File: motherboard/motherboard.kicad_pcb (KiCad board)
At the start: 4 copper layers, 158.5 x 92 mm, 270 parts, among them CN1 PJ-332A-6A (3.5mm Jack), IC1 PI6C557-05BLE, J1 USB_C_Receptacle, J10 DEBUG UART, J11 SYSTEM, J12 5V FAN, J13 Bus_M.2_Socket_E, J14 Micro_SD_Card_Det1, J15 Bus_M.2_Socket_M, J16 USB, J17 USB, J18 USB, J19 USB, J2 20455-040E-76 OLED IPEX, J20 CM3588 Hirose Connector, J21 5V IN, J22 BATTERY IN, J3 RIGHT SPEAKERS, J4 LEFT SPEAKERS, J5 Outer USB-C, J6 OLED EL POWER, J7 HALL SWITCH, J8 HDMI_A, J9 Inner USB-C, Q1 2SK3018W, Q10 2SK3018W, Q11 AO3415A, Q12 2SK3018W, Q2 2SK3018W, Q3 L2N7002WT1G, Q4 2SK3018W, Q5 2SK3018W, Q6 WNM6002-3/TR, Q7 WNM6002-3/TR, Q8 WNM6002-3/TR, Q9 WNM6002-3/TR, SW1 PWR, SW2 RESET, SW3 MASK, SW4 RECOVERY, U1 TPD4E02B04, U10 TPD4E02B04, U11 TPD4E02B04, U12 TPD4E02B04, U13 TPD4E02B04, U14 AP2331, U15 TVS2200DRV, U18 TPD4E02B04, U19 TPD4E02B04, U2 TPD4E02B04, U20 TPS54331DR, U21 AP2127K-3.3, U22 CH334F, U23 TPA2028D1YZFT, U25 TPA2028D1YZFT, U26 AMS1117-1.8, U27 TPS54331DR, U28 SPI Flash, U29 TVS2200DRV, U3 TPD4E02B04, U4 FUSB302BMPX, U5 SY6280AAC, U6 SY6280AAC, U7 FUSB302BMPX, U8 TPD4E02B04, U9 TPD4E02B04, Y1 25MHz, Y2 12MHz

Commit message: routing work
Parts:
- moved R4 11.8 mm to (100.4, 123.7), turned to 90 degrees
- moved C23 1.33 mm to (67.7, 88.2), turned to 0 degrees
- moved R5 0.79 mm to (100.6, 136.7), turned to 180 degrees
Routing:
- net +1V8: track 0.00 -> 37.3 mm, vias 0 -> 2
- net /HDMI_TX/HDMI0_5V: track 0.00 -> 30.3 mm
- net /USBC0/CC1: track 0.00 -> 23.7 mm, vias 0 -> 2
- net /Audio/L_DET: track 0.00 -> 23.0 mm, vias 0 -> 2
- net /USBC0/CC2: track 0.00 -> 22.1 mm, vias 0 -> 2
- net /HDMI_TX/CEC: track 0.00 -> 20.9 mm, vias 0 -> 2
- net Net-(J1-SHIELD): track 0.00 -> 20.7 mm
- net unconnected-(R1-Pad1): track 0.00 -> 19.2 mm
- net /HDMI_TX/SCL: track 0.00 -> 19.2 mm, vias 0 -> 2
- net /USBC1/VBUS: track 7.74 -> 26.9 mm, vias 0 -> 2
- net /USBC1/CC1: track 0.00 -> 18.2 mm, vias 0 -> 2
- net /USBC1/CC2: track 0.00 -> 17.7 mm, vias 0 -> 2
- net /HDMI_TX/SDA: track 0.00 -> 16.2 mm, vias 0 -> 2
- net /USBC0/SBUS2: track 0.00 -> 12.8 mm, vias 0 -> 2
- net /Audio/L_AUDIO: track 0.00 -> 12.8 mm, vias 0 -> 3
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- removed copper zone on F.Cu, net /USBC1/VBUS

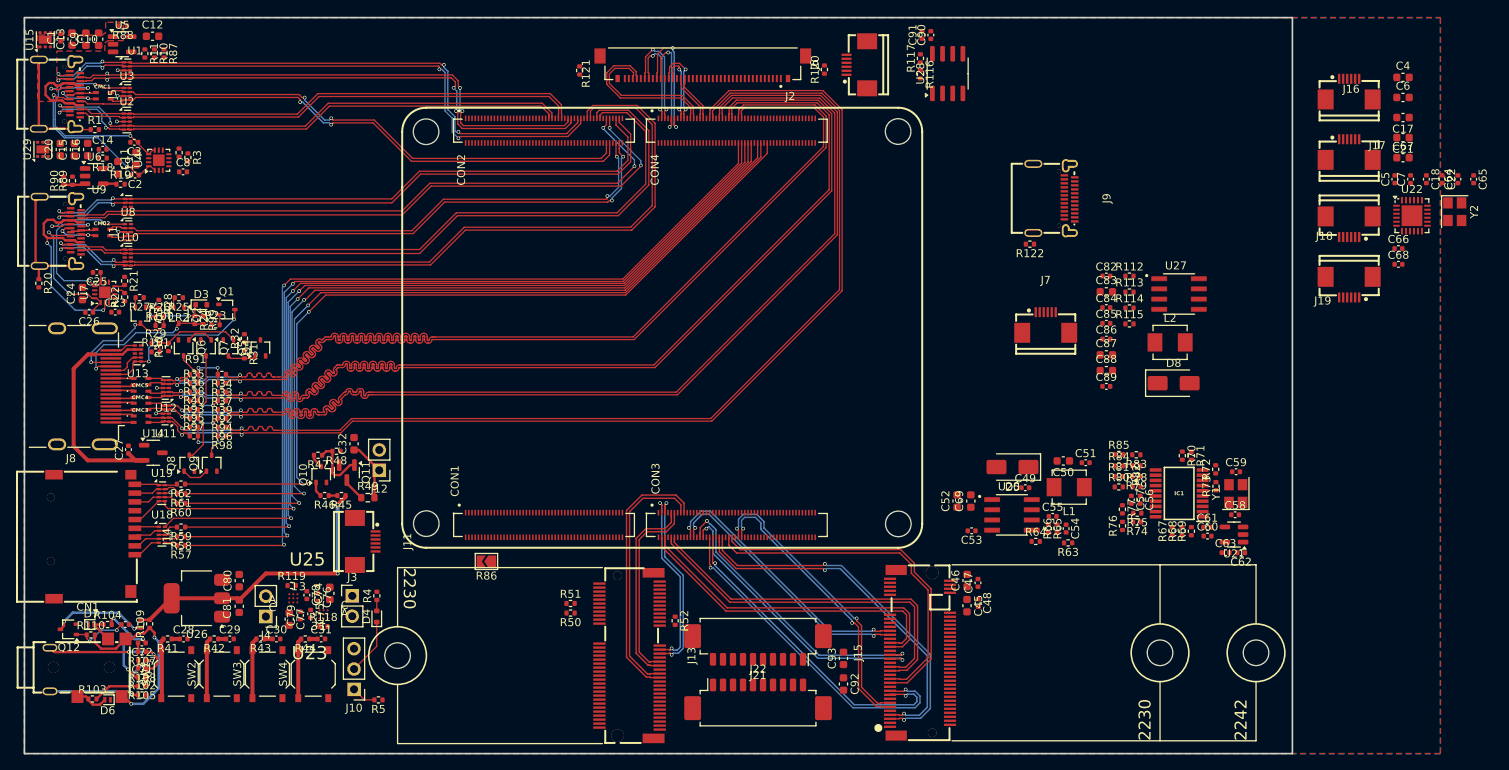
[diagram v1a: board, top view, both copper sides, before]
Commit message: added two more display eval test boards
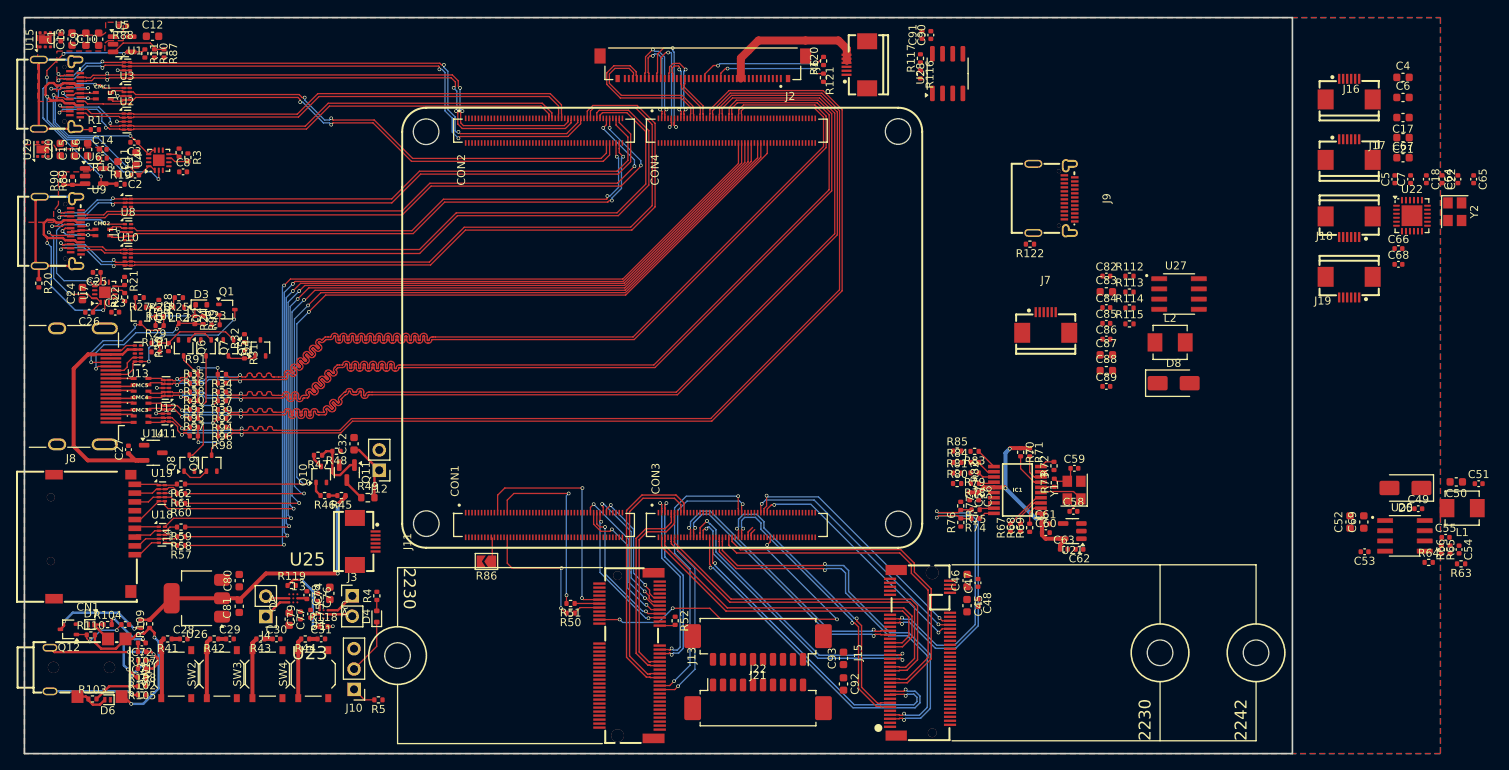
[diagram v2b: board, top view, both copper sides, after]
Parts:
- moved C49 49.2 mm to (230.6, 112.8)
- moved C50 49.2 mm to (235.3, 109.5)
- moved C51 49.2 mm to (238.1, 109.7)
- moved C52 49.2 mm to (222.1, 114.5)
- moved C53 49.2 mm to (223.9, 118.2)
- moved C54 49.2 mm to (235.7, 117.9)
- moved C55 49.2 mm to (234.0, 116.4)
- moved C69 49.2 mm to (223.8, 114.5)
- moved D5 49.2 mm to (229.0, 110.2)
- moved L1 49.2 mm to (236.1, 112.7)
- moved R63 49.2 mm to (235.9, 119.7)
- moved R64 49.2 mm to (231.9, 119.5)
- moved R65 49.2 mm to (233.5, 117.9)
- moved R66 49.2 mm to (234.6, 117.9)
- moved U20 49.2 mm to (228.9, 116.2)
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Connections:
- C45 pad 1: /PCIE3.0-MKEY/+3.3V_PCIE -> +3.3V_PCIE
- C46 pad 1: /PCIE3.0-MKEY/+3.3V_PCIE -> +3.3V_PCIE
- C47 pad 1: /PCIE3.0-MKEY/+3.3V_PCIE -> +3.3V_PCIE
- C48 pad 1: /PCIE3.0-MKEY/+3.3V_PCIE -> +3.3V_PCIE
- C50 pad 1: /PCIE3.0-MKEY/+3.3V_PCIE -> +3.3V_PCIE
- C51 pad 1: /PCIE3.0-MKEY/+3.3V_PCIE -> +3.3V_PCIE
- J13 pad 2: /PCIE2.0-EKEY/EKEY_3.3V -> +3.3V_PCIE
- J13 pad 4: /PCIE2.0-EKEY/EKEY_3.3V -> +3.3V_PCIE
- J13 pad 72: /PCIE2.0-EKEY/EKEY_3.3V -> +3.3V_PCIE
- J13 pad 74: /PCIE2.0-EKEY/EKEY_3.3V -> +3.3V_PCIE
- J15 pad 12: /PCIE3.0-MKEY/+3.3V_PCIE -> +3.3V_PCIE
- J15 pad 14: /PCIE3.0-MKEY/+3.3V_PCIE -> +3.3V_PCIE
- J15 pad 16: /PCIE3.0-MKEY/+3.3V_PCIE -> +3.3V_PCIE
- J15 pad 18: /PCIE3.0-MKEY/+3.3V_PCIE -> +3.3V_PCIE
- J15 pad 2: /PCIE3.0-MKEY/+3.3V_PCIE -> +3.3V_PCIE
- J15 pad 4: /PCIE3.0-MKEY/+3.3V_PCIE -> +3.3V_PCIE
- J15 pad 70: /PCIE3.0-MKEY/+3.3V_PCIE -> +3.3V_PCIE
- J15 pad 72: /PCIE3.0-MKEY/+3.3V_PCIE -> +3.3V_PCIE
- J15 pad 74: /PCIE3.0-MKEY/+3.3V_PCIE -> +3.3V_PCIE
- L1 pad 1: /PCIE3.0-MKEY/+3.3V_PCIE -> +3.3V_PCIE
- R63 pad 1: /PCIE3.0-MKEY/+3.3V_PCIE -> +3.3V_PCIE
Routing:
- net /GPIO0_C5/UART0_TX_M0/PWM4_M0: track 0.00 -> 45.2 mm, vias 0 -> 4
- net /PCIE3.0-MKEY/PCIE30_REFCLK_A_N: track 0.00 -> 37.1 mm, vias 0 -> 2
- net /GPIO4_A1/TP_2_RST_L: track 0.00 -> 36.1 mm, vias 0 -> 2
- net /GPIO4_A0/TP_2_INT_L: track 0.00 -> 35.9 mm, vias 0 -> 2
- net /PCIE3.0-MKEY/PCIE30_REFCLK_A_P: track 0.00 -> 35.8 mm, vias 0 -> 2
- net /GPIO4_B5/PCIE30X4_WAKEn_M1_L: track 0.00 -> 31.7 mm, vias 0 -> 2
- net /GPIO4_B4/PCIE30X4_CLKREQn_M1_L: track 0.00 -> 31.3 mm, vias 0 -> 2
- net /GPIO1_D2/TYPEC5V_PWREN_H: track 1.67 -> 32.7 mm, vias 0 -> 4
- net /GPIO4_B6/PCIE30X4_PERSTn_M1_L: track 0.00 -> 30.4 mm, vias 0 -> 2
- net /GPIO2_C0: track 0.00 -> 29.0 mm, vias 0 -> 2
- net /PCIE3.0-MKEY/+3.3V_PI6C: track 0.00 -> 25.7 mm, vias 0 -> 3
- net /GPIO2_C3: track 0.00 -> 23.5 mm, vias 0 -> 2
- net /USBC0/VBUS: track 12.2 -> 33.2 mm, vias 0 -> 2
- net Net-(J6-Pin_4): track 0.00 -> 18.6 mm
- net /GPIO2_A6: track 0.00 -> 17.9 mm, vias 0 -> 2
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- added copper zone on F.Cu, net /USBC1/VBUS

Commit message: starting motherboard v0.2
lessons from display eval v1
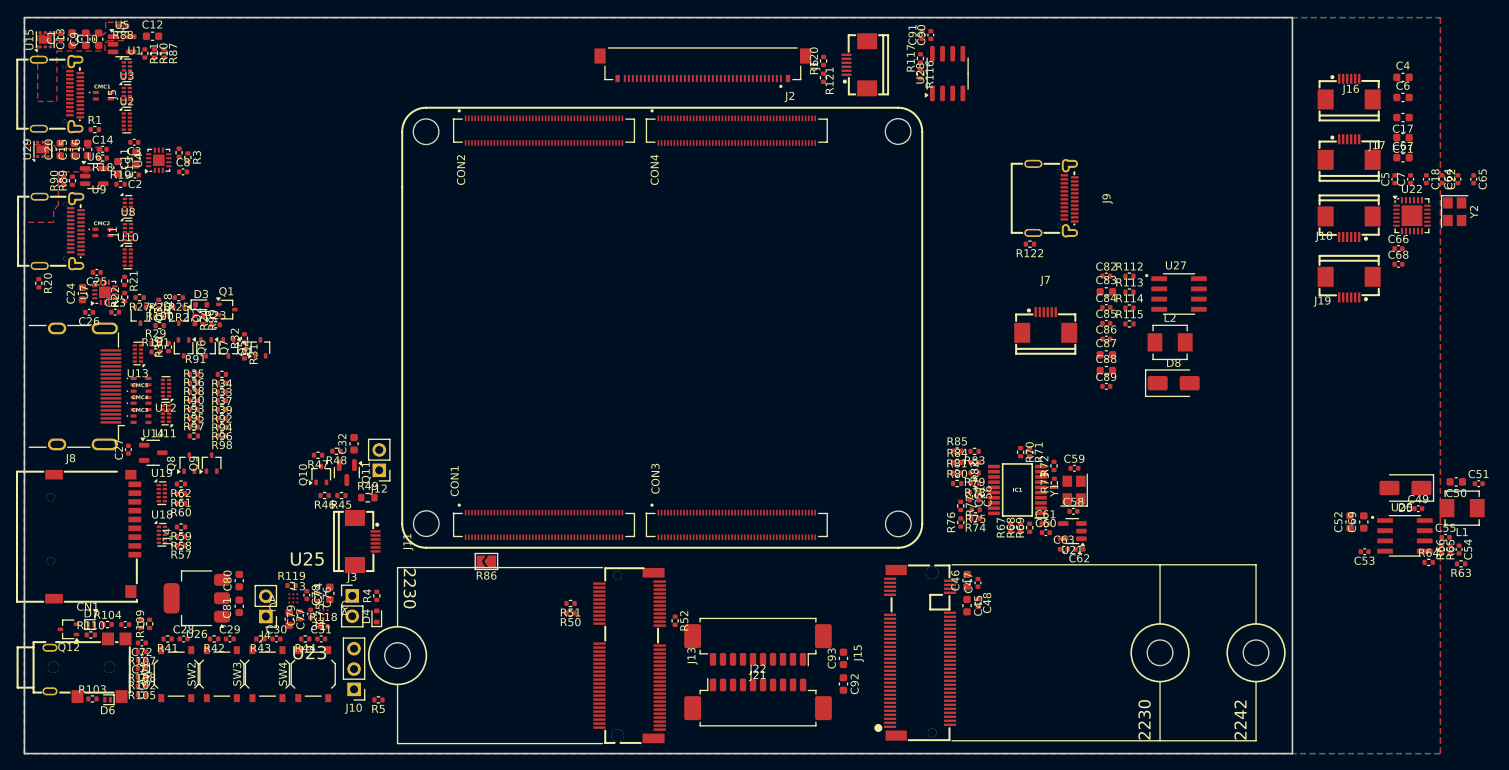
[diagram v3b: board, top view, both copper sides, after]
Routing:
- net /HDMI_TX/HDMI0_TX1P: track 141.2 -> 0.00 mm, vias 2 -> 0
- net /HDMI_TX/HDMI0_TX2P: track 141.1 -> 0.00 mm, vias 2 -> 0
- net /HDMI_TX/HDMI0_TX0P: track 141.0 -> 0.00 mm, vias 2 -> 0
- net /HDMI_TX/HDMI0_TX1N: track 140.9 -> 0.00 mm, vias 2 -> 0
- net /HDMI_TX/HDMI0_TX0N: track 140.8 -> 0.00 mm, vias 2 -> 0
- net /HDMI_TX/HDMI0_TX2N: track 140.7 -> 0.00 mm, vias 2 -> 0
- net /HDMI_TX/HDMI0_TX3P: track 140.5 -> 0.00 mm, vias 2 -> 0
- net /HDMI_TX/HDMI0_TX3N: track 140.2 -> 0.00 mm, vias 2 -> 0
- net /SD Card/CLK: track 114.4 -> 0.00 mm, vias 2 -> 0
- net /SD Card/VDD: track 113.6 -> 0.00 mm, vias 2 -> 0
- net /SDMMC0_D2: track 110.6 -> 0.00 mm, vias 2 -> 0
- net /SDMMC0_D3: track 109.7 -> 0.00 mm, vias 2 -> 0
- net /SDMMC0_CMD: track 108.5 -> 0.00 mm, vias 2 -> 0
- net /SDMMC0_D0: track 106.6 -> 0.00 mm, vias 2 -> 0
- net /SDMMC0_D1: track 105.8 -> 0.00 mm, vias 2 -> 0
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
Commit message: v0.2 layout
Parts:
- removed C54, C85: 1nF, Capacitor_SMD:C_0402_1005Metric
- removed C55, C86: 10pF, Capacitor_SMD:C_0402_1005Metric
- removed C69, C77, C83, C87, C88, C92, C93: 10uF, Capacitor_SMD:C_0603_1608Metric
- removed C78, C79, C84: 1uF, Capacitor_SMD:C_0402_1005Metric
- removed C82: 100nF, Capacitor_SMD:C_0402_1005Metric
- removed C89: 8.2nF, Capacitor_SMD:C_0402_1005Metric
- removed D5, D8: SS54, Diode_SMD:D_SMA
- removed J21: 5V IN, Connector_Molex:Molex_PicoBlade_53261-1071_1x10-1MP_P1.25mm_Horizontal
- removed J9: Inner USB-C, USB-C:USB-C-SMD_TYPE-C-24P-QT
- removed R112, R65: 24k, Resistor_SMD:R_0402_1005Metric
- removed R113, R66: 2k, Resistor_SMD:R_0402_1005Metric
- removed R114, R63: 10k, Resistor_SMD:R_0402_1005Metric
- removed R115, R64: 3.3k, Resistor_SMD:R_0402_1005Metric
- removed R118, R119, R120, R121: 0R, Resistor_SMD:R_0402_1005Metric
- removed R122: 1M, Resistor_SMD:R_0402_1005Metric
- removed U25: TPA2028D1YZFT, Audio_Amp:BGA9C50P3X3_162X162X63
- removed U27: TPS54331DR, TPS54331DR:SOIC127P599X175-8N
- added 10k: Resistor_SMD:R_0402_1005Metric, Resistor_SMD:R_0402_1005Metric, F.Cu at (171.8, 118.4)
- added C33: 1uF, Capacitor_SMD:C_0402_1005Metric, F.Cu at (170.9, 54.3)
- added C34: 1uF, Capacitor_SMD:C_0402_1005Metric, F.Cu at (170.9, 55.4)
- added C35: 1uF, Capacitor_SMD:C_0402_1005Metric, F.Cu at (178.8, 55.1)
- added C36: 1uF, Capacitor_SMD:C_0402_1005Metric, F.Cu at (178.7, 54.0)
- added C37: 10uF, Capacitor_SMD:C_0603_1608Metric, F.Cu at (179.3, 58.1)
- added C38: 0.1uF, Capacitor_SMD:C_0402_1005Metric, F.Cu at (181.5, 56.6)
- added C39: 22uF, Capacitor_SMD:C_0603_1608Metric, F.Cu at (159.9, 72.6)
- added C40: 100nF, Capacitor_SMD:C_0402_1005Metric, F.Cu at (160.4, 71.2)
- added C41: 22uF, Capacitor_SMD:C_0603_1608Metric, F.Cu at (166.7, 71.4)
- added C42: 100nF, Capacitor_SMD:C_0402_1005Metric, F.Cu at (168.3, 69.3)
- added C43: 22uF, Capacitor_SMD:C_0603_1608Metric, F.Cu at (166.8, 73.0)
- added C44: 22uF, Capacitor_SMD:C_0603_1608Metric, F.Cu at (170.6, 73.5)
- added C70: 100nF, Capacitor_SMD:C_0402_1005Metric, F.Cu at (171.2, 72.1)
- added FB1: GZ1608D601TF, Inductor_SMD:L_0603_1608Metric, F.Cu at (179.3, 56.4)
- added L3: MWSA0603S-3R3MT, Inductor_SMD:L_Sunlord_MWSA0603S, F.Cu at (163.0, 66.8)
- added R12: 10k, Resistor_SMD:R_0402_1005Metric, F.Cu at (175.9, 75.3)
- added R13: 220k, Resistor_SMD:R_0402_1005Metric, F.Cu at (173.9, 75.6)
- added R14: 33k, Resistor_SMD:R_0402_1005Metric, F.Cu at (173.8, 74.5)
- added R15: 330k, Resistor_SMD:R_0402_1005Metric, F.Cu at (171.7, 75.0)
- added R16: 10k, Resistor_SMD:R_0402_1005Metric, F.Cu at (177.0, 118.7)
- added R17: 49.9k, Resistor_SMD:R_0402_1005Metric, F.Cu at (174.2, 117.8)
- added R53: 510k, Resistor_SMD:R_0402_1005Metric, F.Cu at (174.2, 118.8)
- added R6: 10k, Resistor_SMD:R_0402_1005Metric, F.Cu at (165.7, 74.4)
- added R7: 10k, Resistor_SMD:R_0402_1005Metric, F.Cu at (163.6, 74.7)
- added R8: 49.9k, Resistor_SMD:R_0402_1005Metric, F.Cu at (163.6, 73.6)
- added R9: 510k, Resistor_SMD:R_0402_1005Metric, F.Cu at (162.0, 74.1)
- added TP1: PWRON, TestPoint:TestPoint_THTPad_1.0x1.0mm_Drill0.5mm, F.Cu at (154.7, 53.7)
- added U16: TPA2016D2RTJR, TPA2016:QFN50P400X400X80-21N, F.Cu at (174.7, 55.6)
- added U17: TPS564257DRLR, TPS564257:SOT50P160X60-6N, F.Cu at (163.4, 71.9)
- C49: value 100nF -> 22uF; footprint Capacitor_SMD:C_0402_1005Metric -> Capacitor_SMD:C_0603_1608Metric
- C50: value 10uF -> 100nF; footprint Capacitor_SMD:C_0603_1608Metric -> Capacitor_SMD:C_0402_1005Metric
- C51, C75: value 1uF -> 22uF; footprint Capacitor_SMD:C_0402_1005Metric -> Capacitor_SMD:C_0603_1608Metric
- C52, C74: value 10uF -> 22uF
- C53: value 8.2nF -> 100nF
- C76: value 1uF -> 100nF
- L1: value 3.3uH -> MWSA0603S-3R3MT; footprint Inductor_SMD:L_Vishay_IHLP-1616 -> Inductor_SMD:L_Sunlord_MWSA0603S
- L2: value 3.3uH -> FXL0630-4R7-M; footprint Inductor_SMD:L_Vishay_IHLP-1616 -> Inductor_SMD:L_Sunlord_MWSA0603S
- U20: value TPS54331DR -> TPS564257DRLR; footprint TPS54331DR:SOIC127P599X175-8N -> TPS564257:SOT50P160X60-6N
- U23: value TPA2028D1YZFT -> TPS564257DRLR; footprint Audio_Amp:BGA9C50P3X3_162X162X63 -> TPS564257:SOT50P160X60-6N
- moved J4 108.0 mm to (172.9, 61.4), turned to -90 degrees
- moved C76 101.4 mm to (179.2, 70.4)
- moved J3 101.0 mm to (176.8, 61.4), turned to 90 degrees
- moved C75 100.8 mm to (177.4, 72.2), turned to 0 degrees
- moved J10 96.8 mm to (158.0, 59.7)
- moved C74 96.6 mm to (177.4, 73.9), turned to 0 degrees
- moved U23 96.5 mm to (174.2, 72.8), turned to 0 degrees
- moved R5 93.9 mm to (155.0, 60.1), turned to 0 degrees
- moved C22 88.0 mm to (150.4, 100.5), turned to 90 degrees
- moved J11 87.8 mm to (162.7, 56.6), turned to 90 degrees
- moved D4 87.7 mm to (155.1, 57.7), turned to -90 degrees
- moved R4 86.7 mm to (154.0, 55.6), turned to 180 degrees
- moved C21 84.7 mm to (151.9, 102.3)
- moved J22 81.7 mm to (186.2, 64.9), turned to 90 degrees
- moved C17 77.1 mm to (161.8, 102.3)
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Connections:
- net /GPIO0_C6/PW M5_M1 renamed /GPIO0_C6/PWM5_M1
- C49 pad 1: Net-(U20-BOOT) -> VDD
- C49 pad 2: Net-(D5-K) -> GND
- C50 pad 1: +3.3V_PCIE -> VDD
- C52 pad 1: +5V -> +3.3V_PCIE
- C53 pad 1: Net-(U20-SS) -> +3.3V_PCIE
- C75 pad 1: /Audio/R_AUDIO -> +5V
- C75 pad 2: Net-(U23-IN+) -> GND
- C76 pad 1: GND -> +5V
- C76 pad 2: Net-(U23-IN-) -> GND
- C80 pad 1: +5V -> +3.3V
- J2 pad 16: Net-(J2-Pad16) -> /eDP/GPIO3_B7
- J2 pad 20: Net-(J2-Pad20) -> unconnected-(J2-Pad20)
- J20 pad 283: /Audio/SPK_EN -> /GPIO1_A7
- L1 pad 1: +3.3V_PCIE -> Net-(U20-SW)
- L1 pad 2: Net-(D5-K) -> +3.3V_PCIE
- L2 pad 1: +3.3V -> Net-(U23-SW)
- L2 pad 2: Net-(D8-K) -> +5V
- U20 pad 1: Net-(U20-BOOT) -> VDD
- U20 pad 2: +5V -> Net-(U20-SW)
- U20 pad 3: /PCIE3.0-MKEY/EN -> GND
- U20 pad 4: Net-(U20-SS) -> Net-(U20-PG)
- U20 pad 5: Net-(U20-VSENSE) -> /PMIC_EXT_EN_OUT
- U26 pad 3: +5V -> +3.3V
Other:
- board size 158.5 x 92 mm -> 132.9 x 92 mm
